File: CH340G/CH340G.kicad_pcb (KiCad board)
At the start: 2 copper layers, 15.5 x 25.4 mm, 25 parts, among them J2 Conn_01x06, P1 USB_C_Plug_USB2.0, U1 CH340G, U2 AP2127K-3.3, Y1 Crystal_GND24

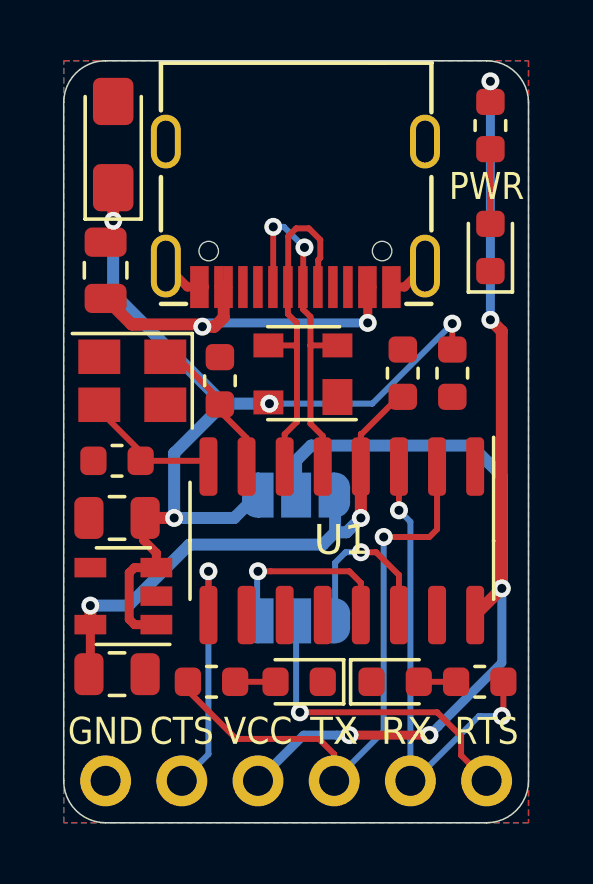
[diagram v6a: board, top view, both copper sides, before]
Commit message: Board Sizes Reduced in Width by 0.254mm
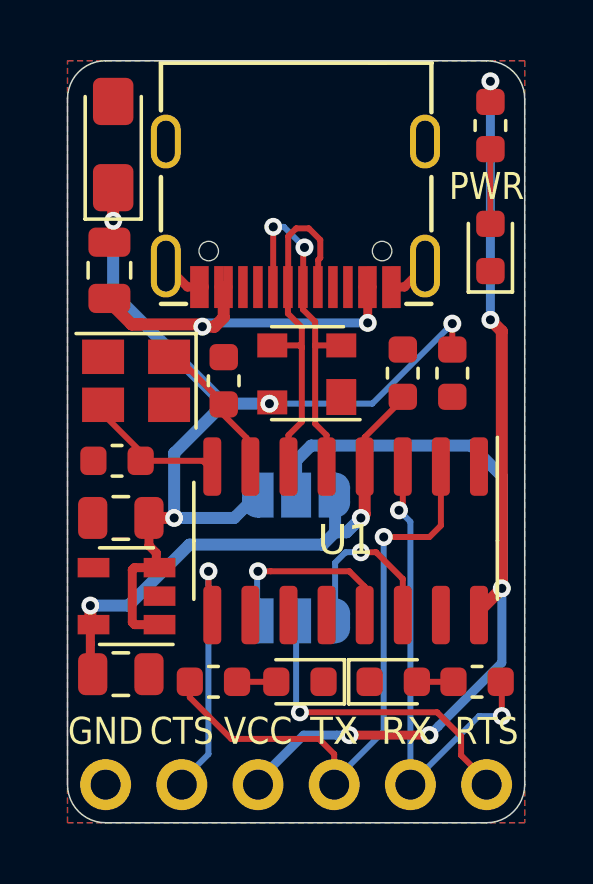
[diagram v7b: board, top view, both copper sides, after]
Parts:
- moved C6 0.13 mm to (64.5, 42.9)
- moved C7 0.13 mm to (64.5, 48.1)
- moved D1 0.13 mm to (70.7, 38.1)
- moved F1 0.13 mm to (64.1, 34.7)
- moved J2 0.13 mm to (76.7, 51.8)
- moved C1 0.13 mm to (67.9, 38.4)
- moved U1 0.13 mm to (72.0, 43.7)
- moved Y1 0.13 mm to (65.0, 38.4)
- moved U2 0.11 mm to (64.7, 45.5)
- moved R3 0.09 mm to (76.4, 48.4)
- moved R2 0.06 mm to (67.6, 48.4)
- moved RX1 0.06 mm to (73.6, 48.4)
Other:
- board size 15.5 x 25.4 mm -> 15.2 x 25.4 mm

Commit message: Soldermask width adjusted
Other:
- rule solder_mask_min_width: 0.1 -> 0.05
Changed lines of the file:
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@@
     (pad_drill 1)
     (pad_to_mask_clearance 0)
-    (solder_mask_min_width 0.1)
+    (solder_mask_min_width 0.05)
     (aux_axis_origin 0 0)
     (visible_elements 7FFFFFFF)
